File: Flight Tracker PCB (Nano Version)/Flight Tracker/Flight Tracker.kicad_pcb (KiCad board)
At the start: 2 copper layers, 101.1 x 78.8 mm, 53 parts, among them J1 Conn_01x02, J2 Conn_01x02, J3 Screw_Terminal_01x02, J4 Conn_01x02, J5 Conn_01x03, J6 Conn_02x03_Odd_Even, Q1 BSS138, Q2 BSS138, Q3 BSS138, Q4 BSS138, Q5 BSS138, Q6 BSS138, Q7 FQP47P06, Q8 BSS138, Q9 BSS138, U1 ML8511, U2 BH1750, U3 SMA_5pin, U4 NTX2, U5 BMP280, U6 MPU_9250, U7 UBlox_MAX8

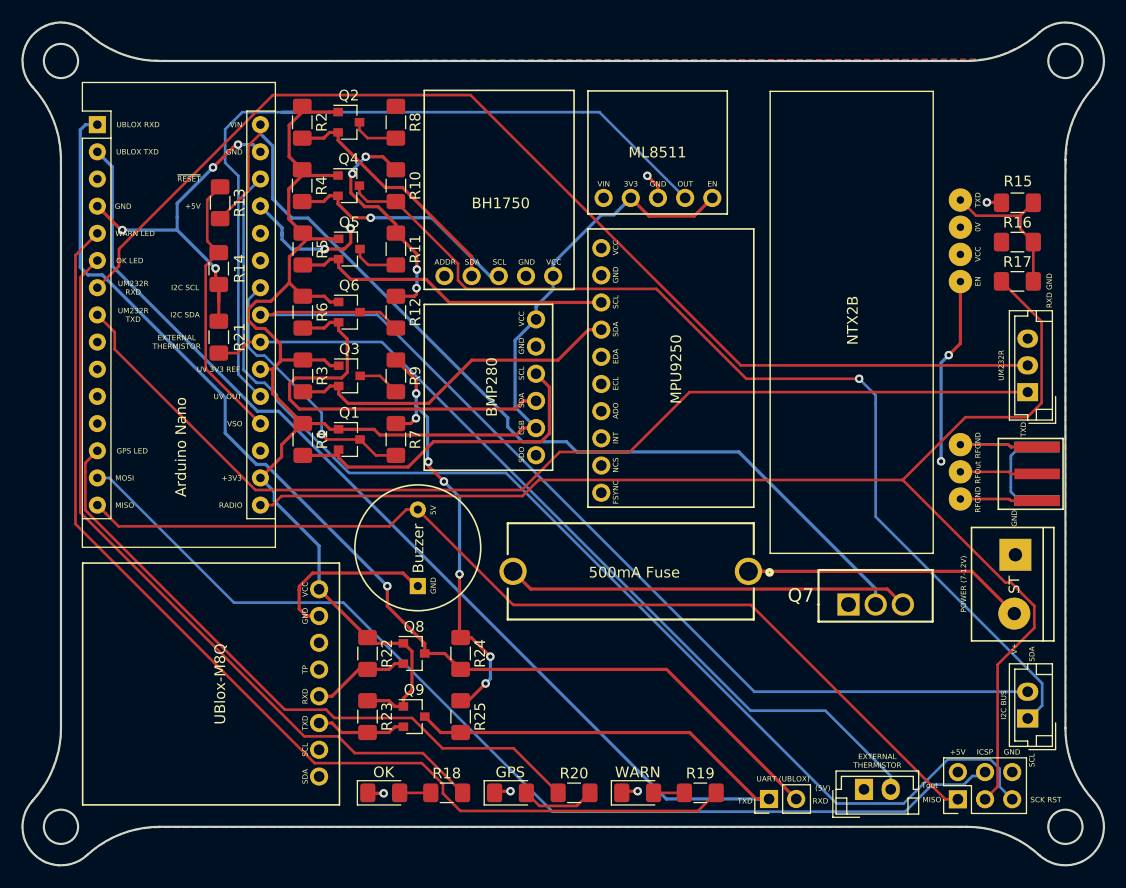
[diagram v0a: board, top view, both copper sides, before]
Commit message: made bmp280 cad model and linked it to pcb, also created sockets for arduino nano
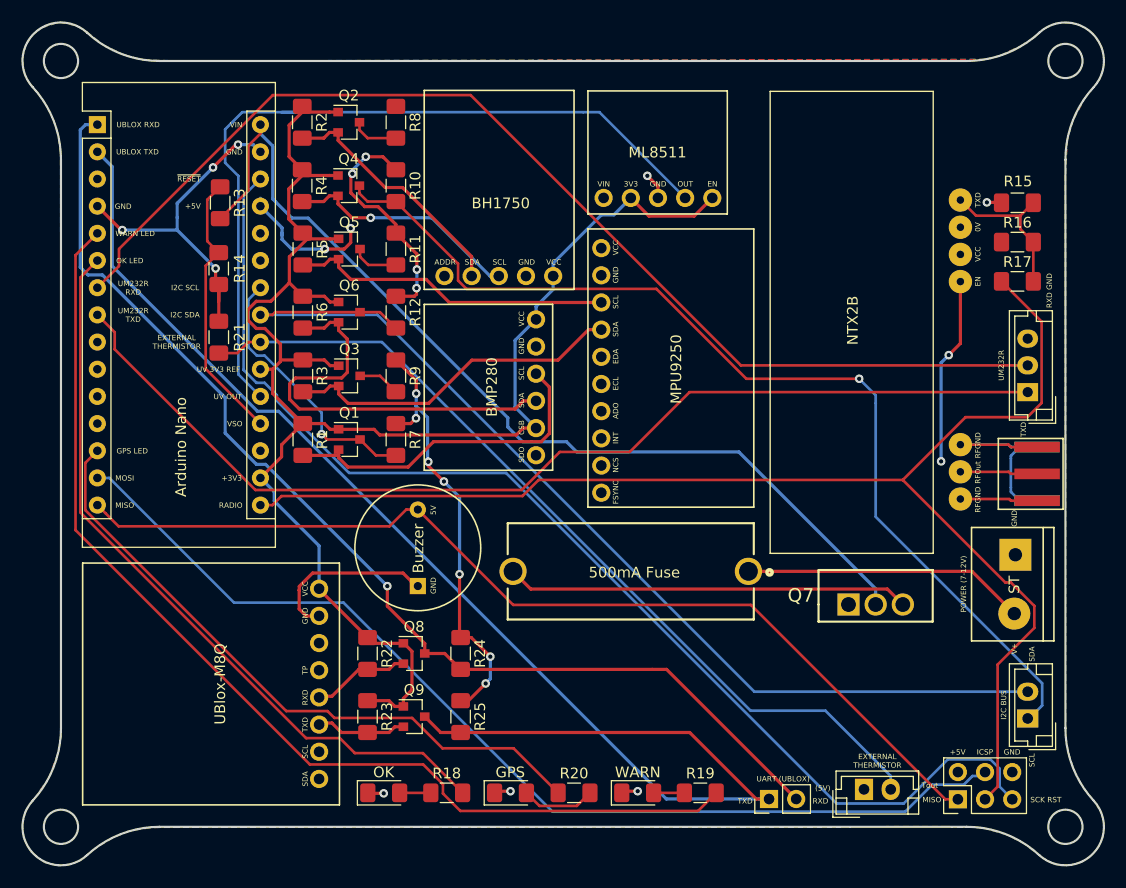
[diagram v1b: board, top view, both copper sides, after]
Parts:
- A1: footprint Module:Arduino_Nano -> NTX2:Arduino_Nano_With_Model
- U4: value NTX2 -> NTX2_With_Model; footprint NTX2:NTX2 -> NTX2:NTX2_With_Model
- U7: footprint NTX2:Ublox Max 8 -> NTX2:ublox_M8Q_with_Model

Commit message: Created fuse holder and linked it with footprint
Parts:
- A1: footprint NTX2:Arduino_Nano_With_Model -> NTX2:Arduino_Nano_With_Model_Sockets
- F1: footprint NTX2:MC000827 -> NTX2:MC000827_With_Model
- U1: value ML8511 -> ML8511_With_Model; footprint NTX2:ML8511 -> NTX2:ML8511_With_Model
- U2: value BH1750 -> BH1750_With_Model; footprint NTX2:BH1750 -> NTX2:BH1750_With_Model
- U5: value BMP280 -> BMP280_With_Model; footprint NTX2:BMP280 -> NTX2:BMP280_With_Model
- U6: value MPU_9250 -> MPU_9250_With_Model; footprint NTX2:MPU_9250 -> NTX2:MPU_9250_With_Model
